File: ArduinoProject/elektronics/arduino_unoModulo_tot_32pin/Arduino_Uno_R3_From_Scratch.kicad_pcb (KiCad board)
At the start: 2 copper layers, 56.9 x 47.8 mm, 35 parts, among them IC401 MC33269ST-5.OT3, J201 POWER, J202 IOL, J203 IOL, J204 IOL, SW601 RESET_SWITCH, U301 74AHC1G04, U302 L298D, U303 74AHC1G04, U402 LP2985-3.3, U601 ATMEGA328P-MU20, X1 DG3XX-04-3.5, X2 DG3XX-02-3.5, X601 CSTCE16MOV53-R0

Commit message: new components
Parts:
- removed R602: 1M, Resistors_SMD:R_0805
- removed X601: CSTCE16MOV53-R0, CSTCE16M0V53ZW-R0:CSTE_G_A
- added C603: 22p, Capacitors_SMD:C_0805, F.Cu at (180.9, 131.6)
- added C604: 22p, Capacitors_SMD:C_0805, F.Cu at (187.9, 119.3)
- added Y601: Crystal, MCRSD16000F183000RR:HC%2f49US-(AT49)_1, F.Cu at (184.1, 123.1)
- J201: footprint Socket_Strips:Socket_Strip_Straight_1x06_Pitch2.00mm -> Socket_Strips:Socket_Strip_Straight_1x06_Pitch2.54mm
- J202, J203, J204: footprint Socket_Strips:Socket_Strip_Straight_1x08_Pitch2.00mm -> Socket_Strips:Socket_Strip_Straight_1x08_Pitch2.54mm
- moved J203 15.5 mm to (205.2, 96.3)
- moved C601 13.9 mm to (202.5, 118.8), turned to 90 degrees
- moved J202 11.7 mm to (205.4, 119.5), turned to 0 degrees
- moved U601 6.50 mm to (194.4, 118.1)
- moved J204 3.94 mm to (176.4, 128.9)
- moved J201 3.05 mm to (187.6, 109.5)
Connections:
- D505 pad 2: /L298_Driver./OUT4 -> /L298_Driver./OUT3
- D506 pad 1: /L298_Driver./OUT4 -> /L298_Driver./OUT3
- D507 pad 2: /L298_Driver./OUT3 -> /L298_Driver./OUT4
- D508 pad 1: /L298_Driver./OUT3 -> /L298_Driver./OUT4
- U302 pad 16: /L298_Driver./OUT4 -> /L298_Driver./OUT3
- U302 pad 17: /L298_Driver./OUT3 -> /L298_Driver./OUT4
- X1 pad 3: /L298_Driver./OUT4 -> /L298_Driver./OUT3
- X1 pad 4: /L298_Driver./OUT3 -> /L298_Driver./OUT4
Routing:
- net GND: track 317.4 -> 245.4 mm
- net 328P_ICSP_MOSI: track 34.4 -> 55.4 mm
- net 328P_ICSP_MISO: track 66.6 -> 85.1 mm
- net 328P_ICSP_SCK: track 54.5 -> 36.8 mm, vias 1 -> 0
- net /ATMEGA328P/IO8: track 6.54 -> 21.0 mm
- net +5V: track 239.5 -> 226.3 mm
- net /ATMEGA328P/IO9: track 6.03 -> 18.7 mm
- net /ATMEGA328P/IO7: track 13.8 -> 24.7 mm
- net /ATMEGA328P/SS: track 5.53 -> 16.4 mm
- net /ATMEGA328P/AREF: track 18.8 -> 7.96 mm, vias 1 -> 0
- net /ATMEGA328P/AD6: track 42.1 -> 52.1 mm
- net /ATMEGA328P/PWMA: track 38.7 -> 47.5 mm
- net /ATMEGA328P/IO4: track 9.46 -> 17.8 mm
- net /ATMEGA328P/IO6: track 13.5 -> 21.3 mm
- net /ATMEGA328P/AD5: track 13.0 -> 20.7 mm
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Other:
- board size 56.9 x 47.8 mm -> 63.8 x 47.8 mm

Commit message: new components2
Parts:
- removed U402: LP2985-3.3, TO_SOT_Packages_SMD:SOT-23-5
- added IC402: MC33269ST-5.OT3, PHT6NQ10T_135:SOT230P700X180-4N, F.Cu at (181.0, 97.6)
- D401: footprint Diodes_SMD:D_0805 -> Diodes_SMD:D_MicroMELF_Hadsoldering
- IC401: footprint MC33269ST-3.3T3G:SOT230P700X175-4N -> PHT6NQ10T_135:SOT230P700X180-4N
- moved C402 4.66 mm to (183.9, 102.4), turned to 180 degrees
- moved D401 3.06 mm to (162.3, 96.7), turned to 270 degrees
- moved IC401 2.79 mm to (171.7, 97.7)
- moved C401 2.78 mm to (180.2, 102.5)
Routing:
- net 328P_ICSP_SCK: track 36.8 -> 100.4 mm, vias 0 -> 1
- net Net-(C603-Pad2): track 5.21 -> 36.8 mm
- net GND: track 245.4 -> 257.7 mm, vias 7 -> 8
- net /Headers/+3V3: track 7.09 -> 15.2 mm
- net /Headers/VIN: track 29.2 -> 36.9 mm
- net +5V: track 226.3 -> 230.5 mm
- net /ATMEGA328P/IO7: track 24.7 -> 21.7 mm
- net /ATMEGA328P/IO6: track 21.3 -> 19.3 mm
- net /L298_Driver./PWRIN: track 110.4 -> 111.8 mm

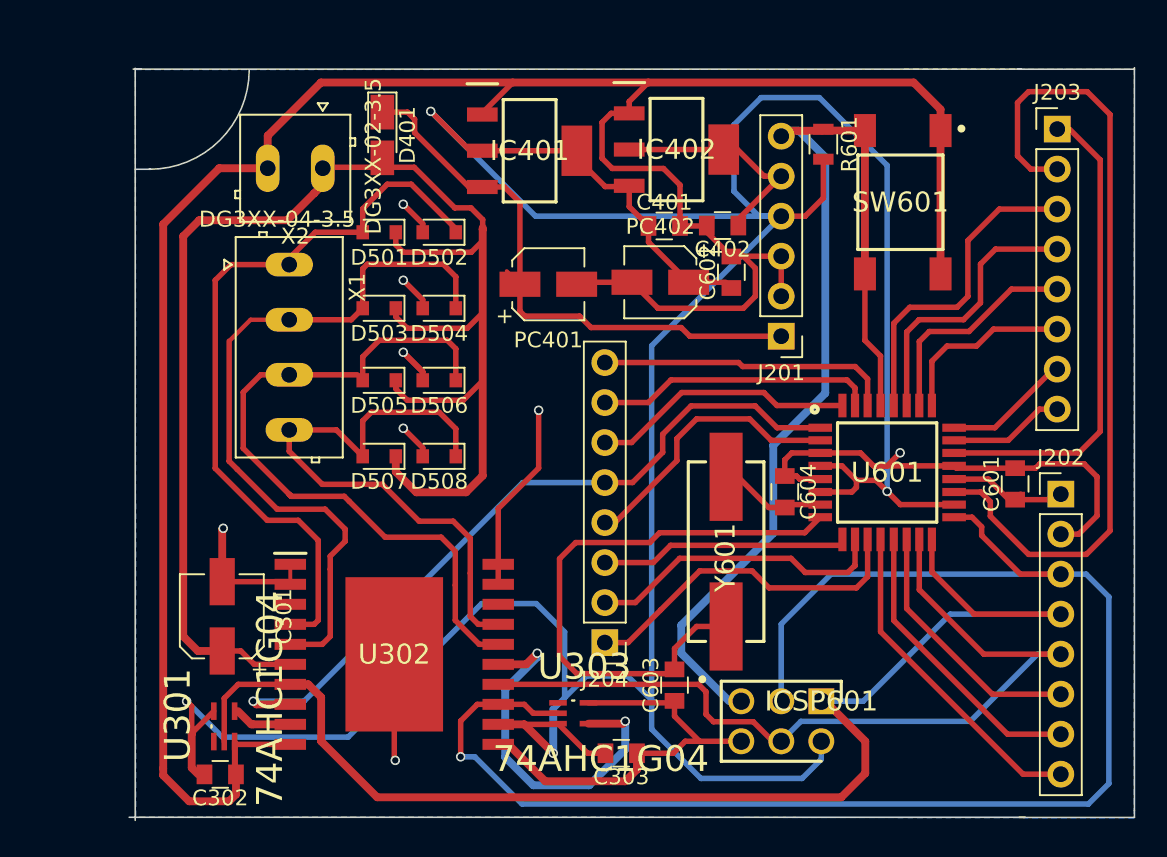
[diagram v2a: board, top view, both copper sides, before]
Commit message: arduino altered
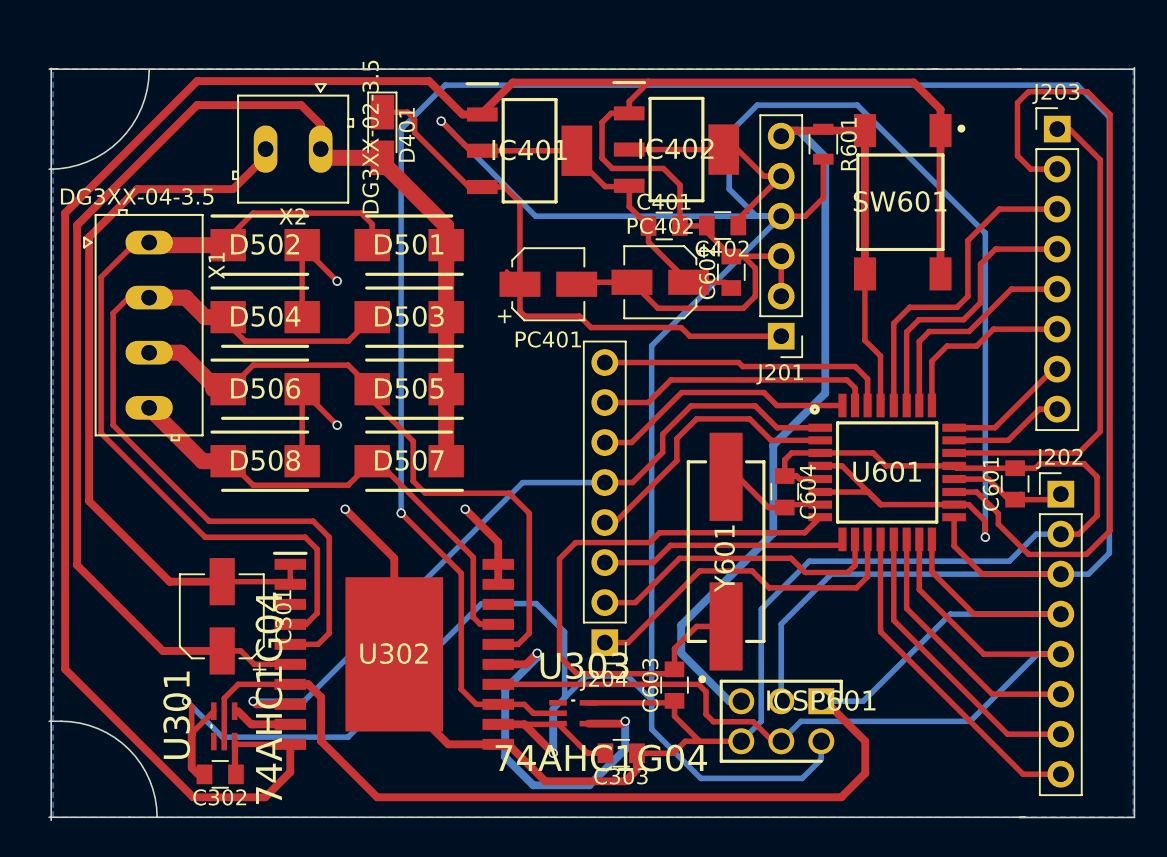
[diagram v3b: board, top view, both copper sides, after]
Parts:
- D501, D502, D503, D504, D505, D506, D507, D508: footprint Diodes_SMD:D_0805 -> SK25AHM2G:DIOM5437X240N
- moved D502 11.1 mm to (154.9, 103.7), turned to 0 degrees
- moved D504 11.1 mm to (154.9, 108.3), turned to 0 degrees
- moved D506 11.1 mm to (154.9, 112.8), turned to 0 degrees
- moved D508 11.1 mm to (154.9, 117.4), turned to 0 degrees
- moved X1 9.00 mm to (147.5, 108.8)
- moved D501 2.07 mm to (164.0, 103.7)
- moved D503 1.98 mm to (164.0, 108.3)
- moved D505 1.98 mm to (164.0, 112.8)
- moved D507 1.93 mm to (164.0, 117.4)
- moved X2 1.22 mm to (156.7, 97.6)
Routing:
- net GND: track 257.7 -> 346.4 mm, vias 8 -> 4
- net 328P_ICSP_SCK: track 100.4 -> 156.4 mm
- net /L298_Driver./PWRIN: track 111.8 -> 83.5 mm
- net +5V: track 230.5 -> 239.8 mm
- net /L298_Driver./OUT4: track 38.7 -> 31.9 mm
- net /L298_Driver./OUT1: track 47.7 -> 53.6 mm
- net /L298_Driver./OUT2: track 46.9 -> 51.5 mm
- net /L298_Driver./OUT3: track 46.3 -> 42.3 mm
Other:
- board size 63.8 x 47.8 mm -> 68.9 x 47.8 mm
- net class fortymill: clearance 1.016 -> 0.2
- net class twentymill: clearance 0.5 -> 0.2

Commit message: baanbreedte verdikt
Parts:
- moved R601 0.40 mm to (190.7, 97.3)
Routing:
- net GND: track 346.4 -> 404.7 mm
- net /ATMEGA328P/RESET: track 69.1 -> 71.2 mm
- net /Headers/VIN: track 36.9 -> 35.2 mm
- net +5V: track 239.8 -> 241.0 mm
- net 328P_ICSP_SCK: track 156.4 -> 155.5 mm
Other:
- outline, holes or cut-outs redrawn
